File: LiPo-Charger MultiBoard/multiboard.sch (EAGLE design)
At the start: 0 parts

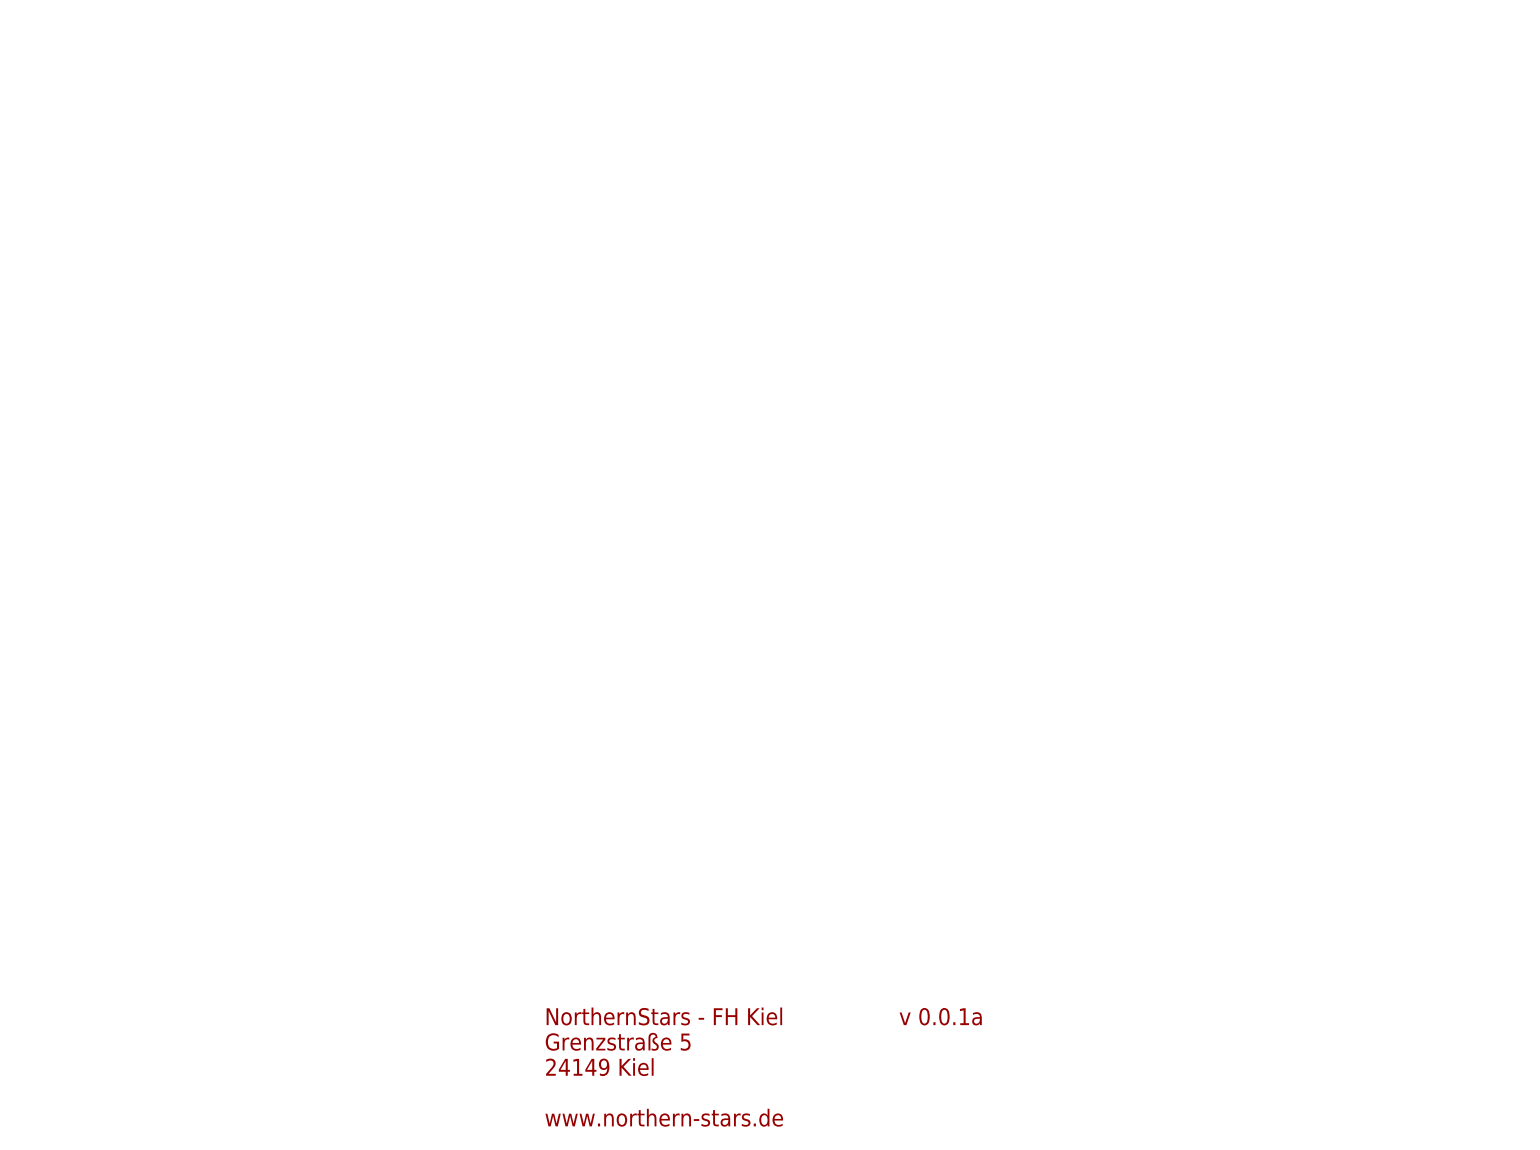
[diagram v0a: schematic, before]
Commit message: Updated LiPo-Charger MultiBoard schematic and board.
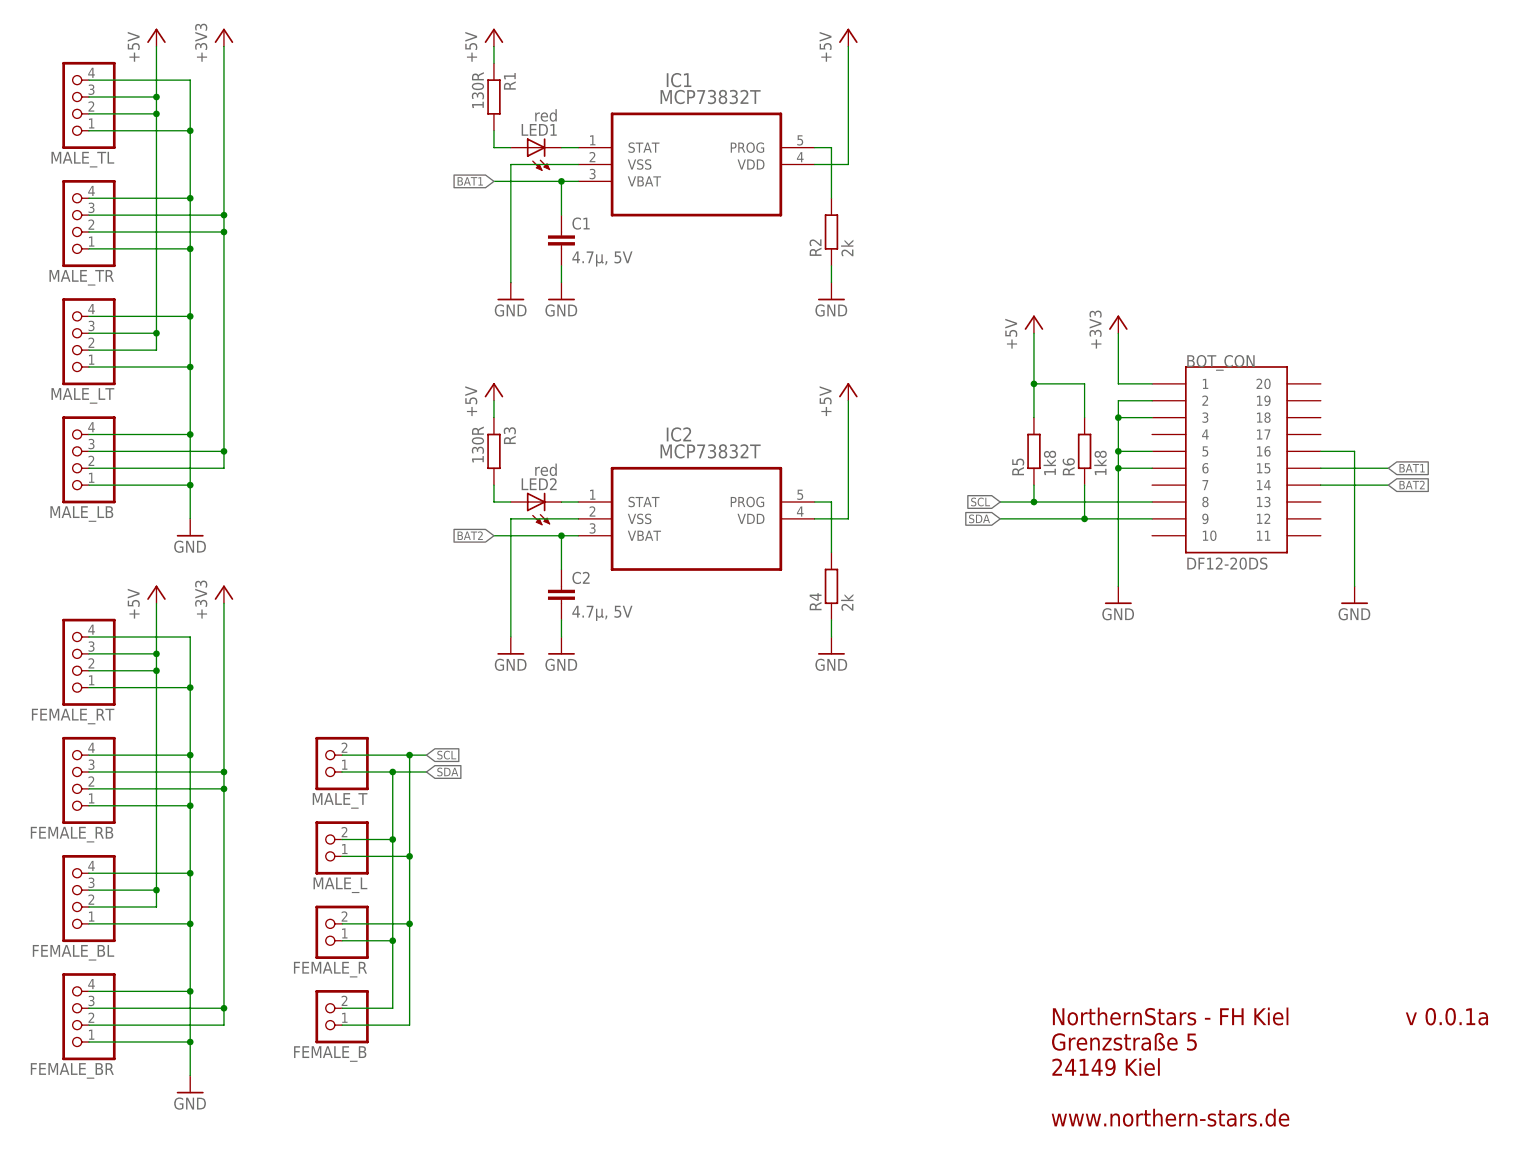
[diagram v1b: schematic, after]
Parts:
- added BOT_CON: DF12-20DS, con-hirose:DF12-20DS
- added C1, C2: 4.7µ, 5V, rcl:C-EUC1206
- added FEMALE_B, FEMALE_R, MALE_L, MALE_T: (no value), pinhead-2:PINHD-1X02_2.54-SMD-90°
- added FEMALE_BL, FEMALE_BR, FEMALE_RB, FEMALE_RT, MALE_LB, MALE_LT, MALE_TL, MALE_TR: (no value), pinhead-2:PINHD-1X04_2.54-SMD-90°
- added IC1, IC2: MCP73832T, microchip:MCP73832T-2DCI/OT
- added LED1, LED2: red, led:LEDCHIPLED_1206
- added R1, R3: 130R, rcl:R-EU_R1206
- added R2, R4: 2k, rcl:R-EU_R1206
- added R5, R6: 1k8, rcl:R-EU_R1206
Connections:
- new net +3V3: BOT_CON.1, FEMALE_BR.2, FEMALE_BR.3, FEMALE_RB.2, FEMALE_RB.3, MALE_LB.2, MALE_LB.3, MALE_TR.2, MALE_TR.3
- new net +5V: FEMALE_BL.2, FEMALE_BL.3, FEMALE_RT.2, FEMALE_RT.3, IC1.VDD, IC2.VDD, MALE_LT.2, MALE_LT.3, MALE_TL.2, MALE_TL.3, R1.1, R3.1, R5.2, R6.2
- new net BAT1: BOT_CON.15, C1.1, IC1.VBAT
- new net BAT2: BOT_CON.14, C2.1, IC2.VBAT
- new net GND: BOT_CON.16, BOT_CON.2, BOT_CON.3, BOT_CON.5, BOT_CON.6, C1.2, C2.2, FEMALE_BL.1, FEMALE_BL.4, FEMALE_BR.1, FEMALE_BR.4, FEMALE_RB.1, FEMALE_RB.4, FEMALE_RT.1, FEMALE_RT.4, IC1.VSS, IC2.VSS, MALE_LB.1, MALE_LB.4, MALE_LT.1, MALE_LT.4, MALE_TL.1, MALE_TL.4, MALE_TR.1, MALE_TR.4, R2.1, R4.1
- new net N$1: IC1.STAT, LED1.C
- new net N$2: LED1.A, R1.2
- new net N$3: IC2.STAT, LED2.C
- new net N$4: IC1.PROG, R2.2
- new net N$5: LED2.A, R3.2
- new net N$6: IC2.PROG, R4.2
- new net SCL: BOT_CON.8, FEMALE_B.1, FEMALE_R.2, MALE_L.1, MALE_T.2, R5.1
- new net SDA: BOT_CON.9, FEMALE_B.2, FEMALE_R.1, MALE_L.2, MALE_T.1, R6.1
